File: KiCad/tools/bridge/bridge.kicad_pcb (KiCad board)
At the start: 4 copper layers, 48 x 55 mm, 74 parts, among them J1 XF2J-1824-12A, J2 XF2J-1824-12A

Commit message: lot of modification, preparing a refactor + some rendering
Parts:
- added G***: LOGO, LOGO, B.Cu at (111.0, 90.0)
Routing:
- added copper zone on In1.Cu, net (none)
- added copper zone on In2.Cu, net (none)
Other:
- board text added: "ClvHd Bridge v1.0"
- board text added: "by aightech"

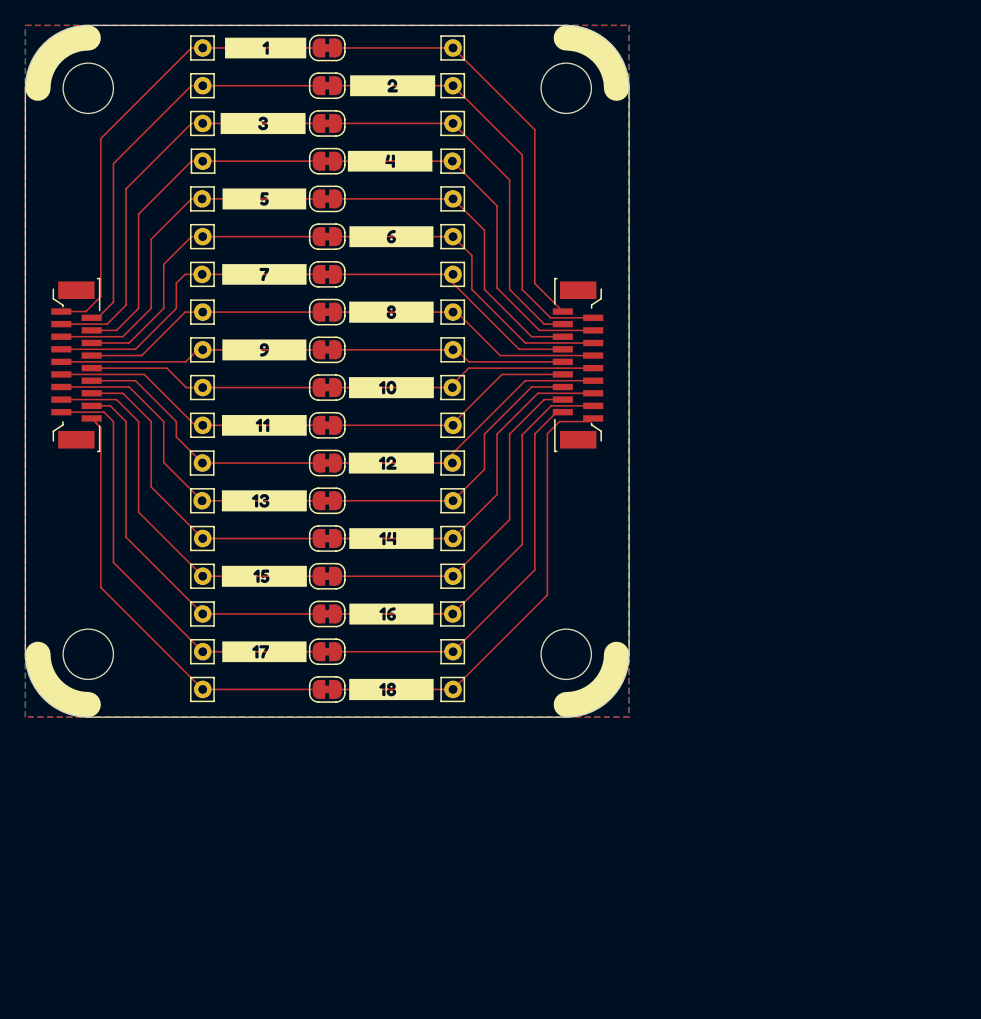
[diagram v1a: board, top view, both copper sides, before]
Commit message: updated bridge
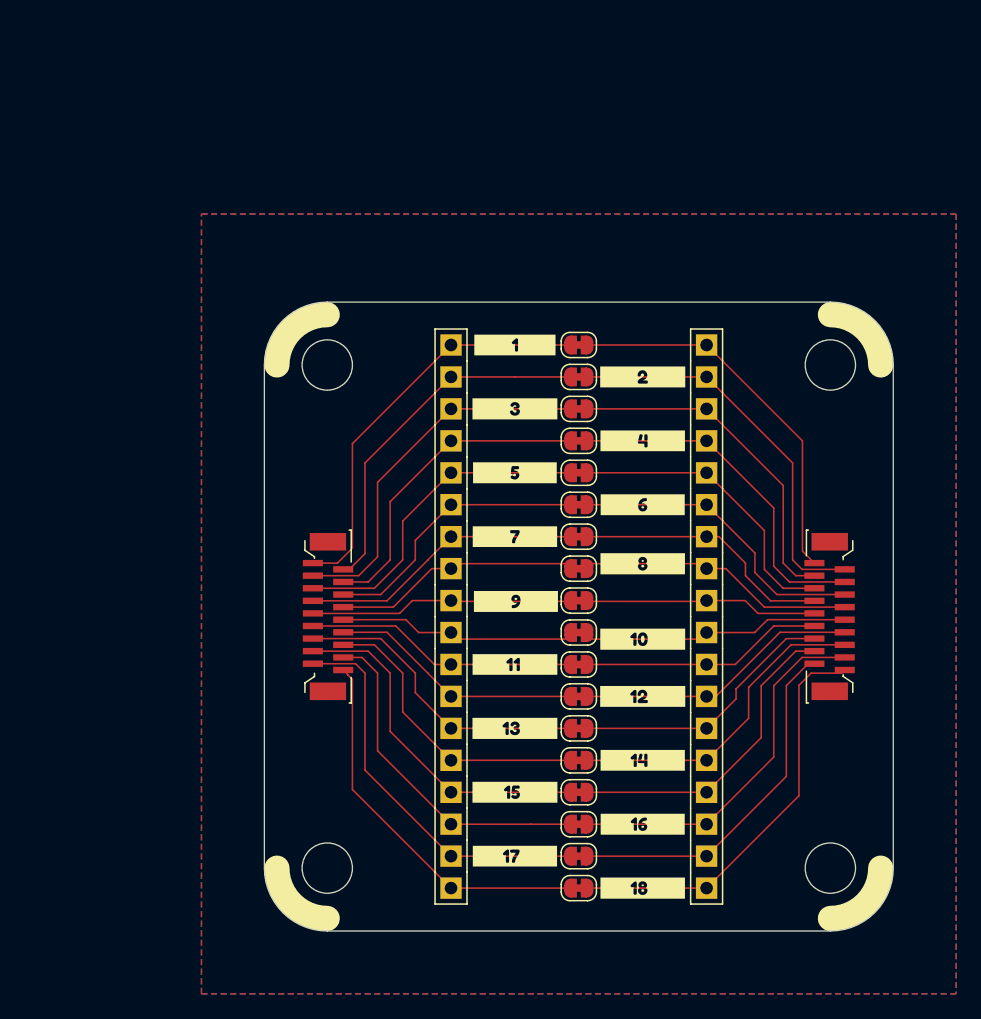
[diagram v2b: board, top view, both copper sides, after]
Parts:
- TP1, TP10, TP11, TP12, TP13, TP14, TP15, TP16, TP17, TP18, TP19, TP2, TP20, TP21, TP22, TP23, TP24, TP25, TP26, TP27, TP28, TP29, TP3, TP30, TP31, TP32, TP33, TP34, TP35, TP36, TP4, TP5, TP6, TP7, TP8, TP9: footprint Connector_Pin:Pin_D0.7mm_L6.5mm_W1.8mm_FlatFork -> Connector_PinHeader_2.54mm:PinHeader_1x01_P2.54mm_Vertical
- moved TP1 31.0 mm to (140.2, 88.4), turned to 180 degrees
- moved JP1 30.9 mm to (130.0, 88.4)
- moved kibuzzard-63B56CBF 30.8 mm to (124.9, 88.4)
- moved TP19 30.8 mm to (119.8, 88.4)
- moved TP2 30.7 mm to (140.2, 91.0), turned to 180 degrees
- moved JP2 30.6 mm to (130.0, 91.0)
- moved kibuzzard-63B56F80 30.5 mm to (135.1, 91.0)
- moved TP20 30.4 mm to (119.8, 91.0)
- moved TP3 30.4 mm to (140.2, 93.5), turned to 180 degrees
- moved kibuzzard-63B56D06 30.3 mm to (124.9, 93.5)
- moved JP3 30.3 mm to (130.0, 93.5)
- moved TP21 30.1 mm to (119.8, 93.5)
- moved TP4 30.0 mm to (140.2, 96.0)
- moved kibuzzard-63B56F84 30.0 mm to (135.1, 96.0)
- moved JP4 29.9 mm to (130.0, 96.0)
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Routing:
- net Net-(JP18-A): track 37.3 -> 32.8 mm
- net Net-(JP17-A): track 32.7 -> 28.6 mm
- net Net-(JP16-A): track 33.1 -> 29.3 mm
- net Net-(JP1-A): track 34.2 -> 30.4 mm
- net Net-(JP1-B): track 36.3 -> 32.5 mm
- net Net-(JP18-B): track 34.1 -> 30.4 mm
- net Net-(JP2-A): track 34.7 -> 31.3 mm
- net Net-(JP2-B): track 31.9 -> 28.6 mm
- net Net-(JP17-B): track 34.5 -> 31.3 mm
- net Net-(JP15-A): track 28.3 -> 25.1 mm
- net Net-(JP3-A): track 30.0 -> 27.2 mm
- net Net-(JP3-B): track 32.3 -> 29.5 mm
- net Net-(JP14-A): track 28.5 -> 25.7 mm
- net Net-(JP16-B): track 29.9 -> 27.2 mm
- net Net-(JP13-A): track 23.9 -> 21.5 mm
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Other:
- board size 48 x 55 mm -> 50 x 50 mm
